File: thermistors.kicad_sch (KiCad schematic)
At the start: 10 parts, among them J3 THERM_1, J4 THERM_2, U7 TCA9535PWR

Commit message: bom: Cleanup some BOM fields
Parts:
- J3: value THERM_1 -> Conn_02x10_Odd_Even
- J4: value THERM_2 -> Conn_02x10_Odd_Even
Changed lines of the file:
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@@
 			)
 		)
-		(property "Value" "THERM_1"
+		(property "Value" "Conn_02x10_Odd_Even"
 			(at 209.55 69.85 0)
 			(effects
@@
 			)
 		)
-		(property "Value" "THERM_2"
+		(property "Value" "Conn_02x10_Odd_Even"
 			(at 209.55 97.79 0)
 			(effects

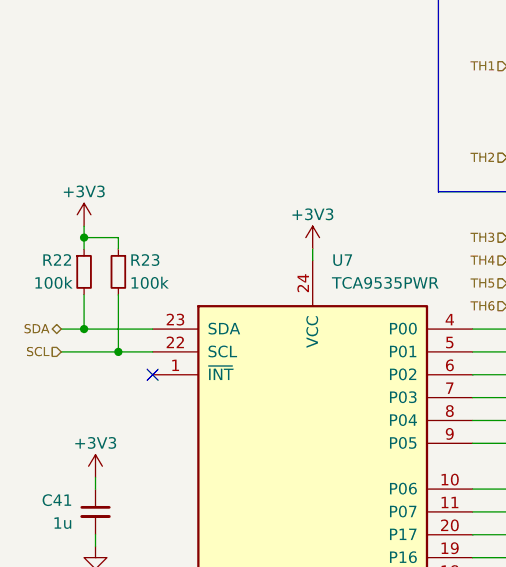
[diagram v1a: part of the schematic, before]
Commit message: schematic: Change all 100k resistors to 10k
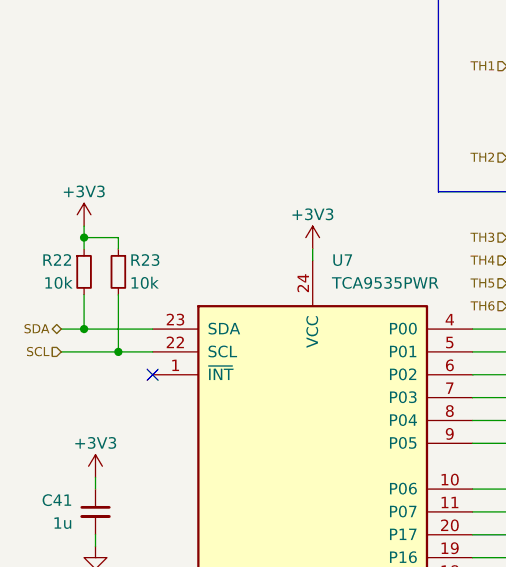
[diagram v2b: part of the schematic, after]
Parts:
- R22, R23: value 100k -> 10k; Dist # C25803 -> C25804; Mfr # 0603WAF1003T5E -> 0603WAF1002T5E
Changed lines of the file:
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@@
 			)
 		)
-		(property "Value" "100k"
+		(property "Value" "10k"
 			(at 153.67 78.74 0)
 			(effects
@@
 			)
 		)
-		(property "Dist #" "C25803"
+		(property "Dist #" "C25804"
 			(at 154.94 77.47 0)
 			(effects
@@
 			)
 		)
-		(property "Mfr #" "0603WAF1003T5E"
+		(property "Mfr #" "0603WAF1002T5E"
 			(at 154.94 77.47 0)
 			(effects
@@
 			)
 		)
-		(property "Value" "100k"
+		(property "Value" "10k"
 			(at 160.02 78.74 0)
 			(effects
@@
 			)
 		)
-		(property "Dist #" "C25803"
+		(property "Dist #" "C25804"
 			(at 158.75 77.47 0)
 			(effects
@@
 			)
 		)
-		(property "Mfr #" "0603WAF1003T5E"
-			(at 158.75 77.47 0)
-			(effects
+		(property "Mfr #" "0603WAF1002T5E"
+			(at 158.75 77.47 0)
+			(effects

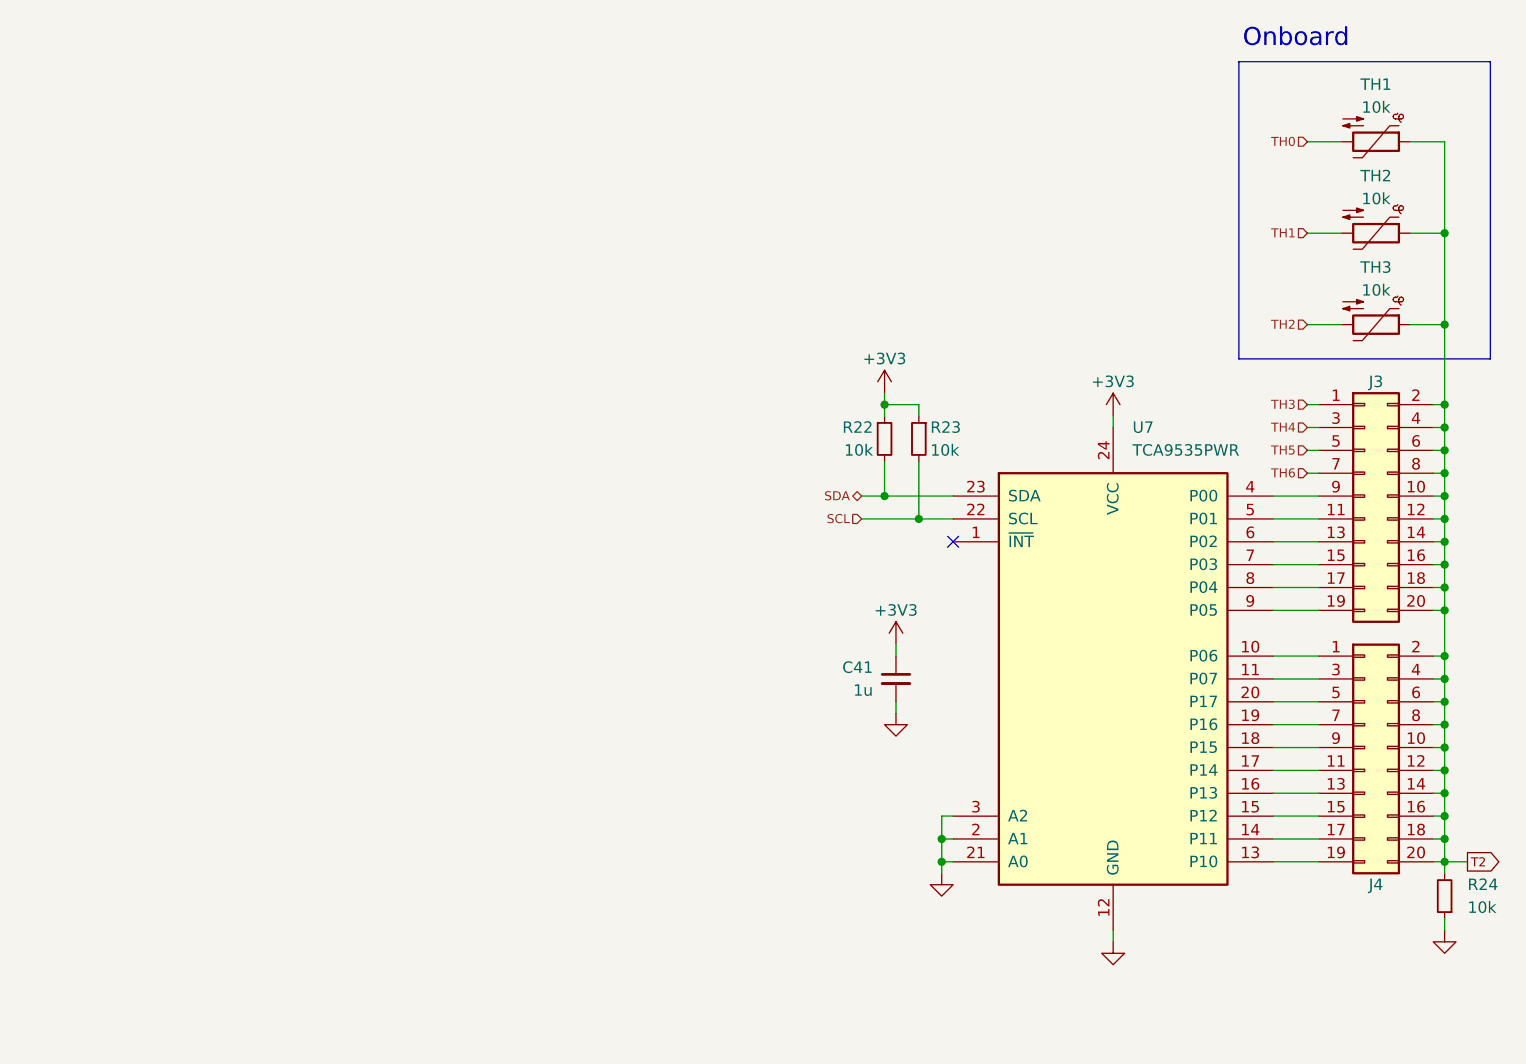
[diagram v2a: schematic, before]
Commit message: schematic: Rework thermistor frontend
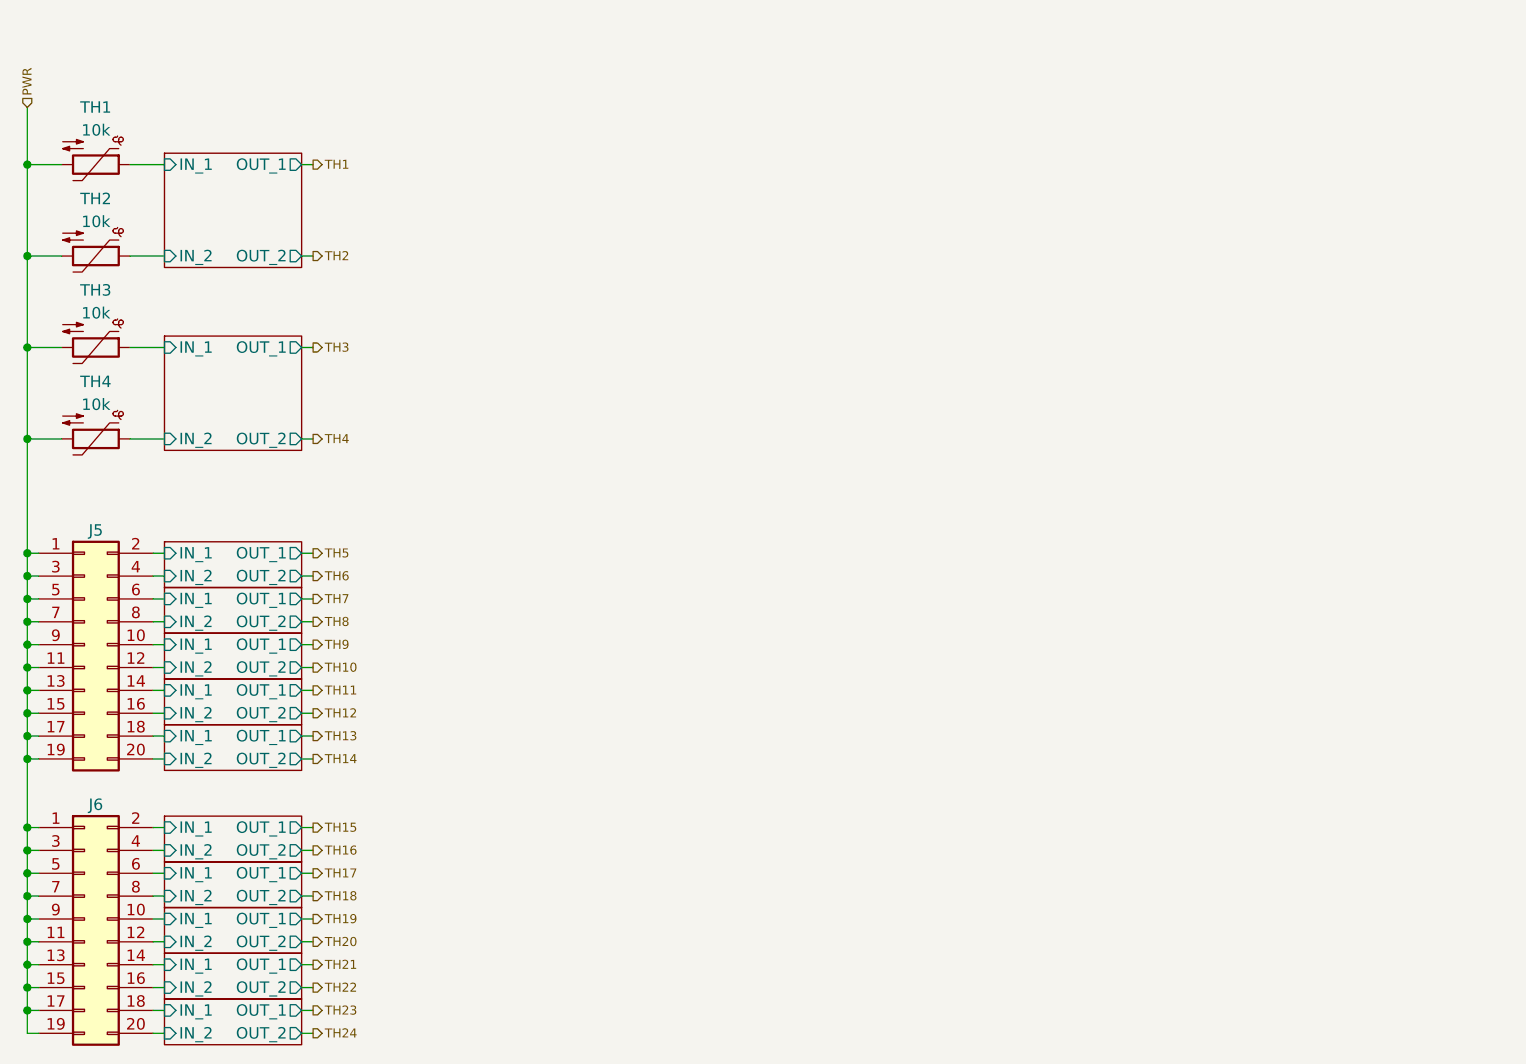
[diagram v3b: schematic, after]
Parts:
- removed C41: 1u, Capacitor_SMD:C_0603_1608Metric, symbol Device:C_Small
- removed J3, J4: Conn_02x10_Odd_Even, Connector_JST:JST_PUD_S20B-PUDSS-1_2x10_P2.00mm_Horizontal, symbol Connector_Generic:Conn_02x10_Odd_Even
- removed R22, R23, R24: 10k, Resistor_SMD:R_0603_1608Metric, symbol Device:R_Small
- removed U7: TCA9535PWR, Package_SO:TSSOP-24_4.4x7.8mm_P0.65mm, symbol Interface_Expansion:TCA9535PWR
- added J5, J6: Conn_02x10_Odd_Even, Connector_JST:JST_PUD_S20B-PUDSS-1_2x10_P2.00mm_Horizontal, symbol Connector_Generic:Conn_02x10_Odd_Even
- added TH4: 10k, Resistor_SMD:R_0603_1608Metric, symbol Device:Thermistor_NTC
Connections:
- net TH1: no longer TH2.2
- net TH2: no longer TH3.2
- removed net T2: TH1.1, TH2.1, TH3.1
- net TH0 renamed PWR
- net PWR: now also TH2.2, TH3.2, J5.1 (Pin_1), J5.11 (Pin_11), J5.13 (Pin_13), J5.15 (Pin_15), J5.17 (Pin_17), J5.19 (Pin_19), J5.3 (Pin_3), J5.5 (Pin_5), J5.7 (Pin_7), J5.9 (Pin_9), J6.1 (Pin_1), J6.11 (Pin_11), J6.13 (Pin_13), J6.15 (Pin_15), J6.17 (Pin_17), J6.19 (Pin_19), J6.3 (Pin_3), J6.5 (Pin_5), J6.7 (Pin_7), J6.9 (Pin_9), TH4.2
- new net Network/IN_1: TH1.1
- new net Network/IN_2: TH2.1
- new net Network1/IN_1: TH3.1
- new net Network1/IN_2: TH4.1
- new net Network10/IN_1: J6.14 (Pin_14)
- new net Network10/IN_2: J6.16 (Pin_16)
- new net Network11/IN_1: J6.18 (Pin_18)
- new net Network11/IN_2: J6.20 (Pin_20)
- new net Network2/IN_1: J5.2 (Pin_2)
- new net Network2/IN_2: J5.4 (Pin_4)
- new net Network3/IN_1: J5.6 (Pin_6)
- new net Network3/IN_2: J5.8 (Pin_8)
- new net Network4/IN_1: J5.10 (Pin_10)
- new net Network4/IN_2: J5.12 (Pin_12)
- new net Network5/IN_1: J5.14 (Pin_14)
- new net Network5/IN_2: J5.16 (Pin_16)
- new net Network6/IN_1: J5.18 (Pin_18)
- new net Network6/IN_2: J5.20 (Pin_20)
- new net Network7/IN_1: J6.2 (Pin_2)
- new net Network7/IN_2: J6.4 (Pin_4)
- new net Network8/IN_1: J6.6 (Pin_6)
- new net Network8/IN_2: J6.8 (Pin_8)
- new net Network9/IN_1: J6.10 (Pin_10)
- new net Network9/IN_2: J6.12 (Pin_12)
- no-connect marks 1 -> 0
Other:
- added sheet Network (thermistor_network.kicad_sch)
- added sheet Network1 (thermistor_network.kicad_sch)
- added sheet Network10 (thermistor_network.kicad_sch)
- added sheet Network11 (thermistor_network.kicad_sch)
- added sheet Network2 (thermistor_network.kicad_sch)
- added sheet Network3 (thermistor_network.kicad_sch)
- added sheet Network4 (thermistor_network.kicad_sch)
- added sheet Network5 (thermistor_network.kicad_sch)
- added sheet Network6 (thermistor_network.kicad_sch)
- added sheet Network7 (thermistor_network.kicad_sch)
- added sheet Network8 (thermistor_network.kicad_sch)
- added sheet Network9 (thermistor_network.kicad_sch)
- note removed: "Onboard"
- title: Battery Management System -> (none)

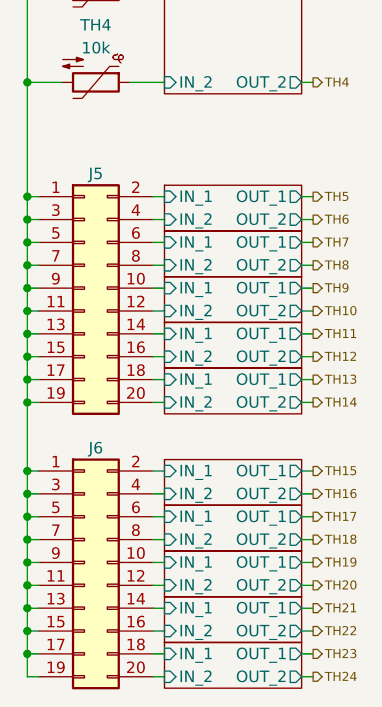
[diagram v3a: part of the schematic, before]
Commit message: schematic: Add board interconnect connectors
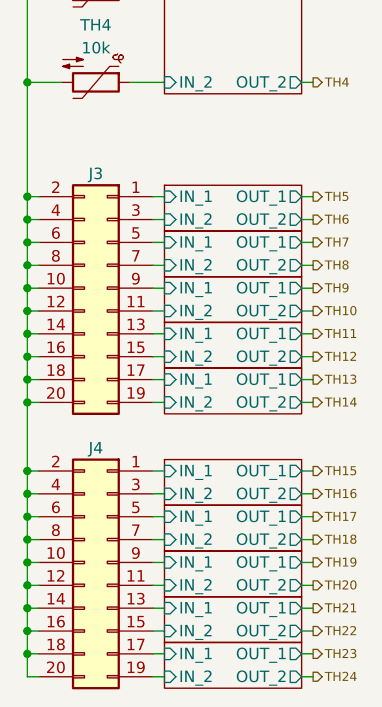
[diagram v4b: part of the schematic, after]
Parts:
- renumbered J5 to J3, J6 to J4
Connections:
- net Network10/IN_1: now also J4.13 (Pin_13); no longer J4.14 (Pin_14)
- net Network10/IN_2: now also J4.15 (Pin_15); no longer J4.16 (Pin_16)
- net Network11/IN_1: now also J4.17 (Pin_17); no longer J4.18 (Pin_18)
- net Network11/IN_2: now also J4.19 (Pin_19); no longer J4.20 (Pin_20)
- net Network2/IN_1: now also J3.1 (Pin_1); no longer J3.2 (Pin_2)
- net Network2/IN_2: now also J3.3 (Pin_3); no longer J3.4 (Pin_4)
- net Network3/IN_1: now also J3.5 (Pin_5); no longer J3.6 (Pin_6)
- net Network3/IN_2: now also J3.7 (Pin_7); no longer J3.8 (Pin_8)
- net Network4/IN_1: now also J3.9 (Pin_9); no longer J3.10 (Pin_10)
- net Network4/IN_2: now also J3.11 (Pin_11); no longer J3.12 (Pin_12)
- net Network5/IN_1: now also J3.13 (Pin_13); no longer J3.14 (Pin_14)
- net Network5/IN_2: now also J3.15 (Pin_15); no longer J3.16 (Pin_16)
- net Network6/IN_1: now also J3.17 (Pin_17); no longer J3.18 (Pin_18)
- net Network6/IN_2: now also J3.19 (Pin_19); no longer J3.20 (Pin_20)
- net Network7/IN_1: now also J4.1 (Pin_1); no longer J4.2 (Pin_2)
- net Network7/IN_2: now also J4.3 (Pin_3); no longer J4.4 (Pin_4)
- net Network8/IN_1: now also J4.5 (Pin_5); no longer J4.6 (Pin_6)
- net Network8/IN_2: now also J4.7 (Pin_7); no longer J4.8 (Pin_8)
- net Network9/IN_1: now also J4.9 (Pin_9); no longer J4.10 (Pin_10)
- net Network9/IN_2: now also J4.11 (Pin_11); no longer J4.12 (Pin_12)
- net PWR: now also J3.10 (Pin_10), J3.12 (Pin_12), J3.14 (Pin_14), J3.16 (Pin_16), J3.18 (Pin_18), J3.2 (Pin_2), J3.20 (Pin_20), J3.4 (Pin_4), J3.6 (Pin_6), J3.8 (Pin_8), J4.10 (Pin_10), J4.12 (Pin_12), J4.14 (Pin_14), J4.16 (Pin_16), J4.18 (Pin_18), J4.2 (Pin_2), J4.20 (Pin_20), J4.4 (Pin_4), J4.6 (Pin_6), J4.8 (Pin_8); no longer J3.1 (Pin_1), J3.11 (Pin_11), J3.13 (Pin_13), J3.15 (Pin_15), J3.17 (Pin_17), J3.19 (Pin_19), J3.3 (Pin_3), J3.5 (Pin_5), J3.7 (Pin_7), J3.9 (Pin_9), J4.1 (Pin_1), J4.11 (Pin_11), J4.13 (Pin_13), J4.15 (Pin_15), J4.17 (Pin_17), J4.19 (Pin_19), J4.3 (Pin_3), J4.5 (Pin_5), J4.7 (Pin_7), J4.9 (Pin_9)
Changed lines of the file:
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@@
 	(symbol
 		(lib_id "Connector_Generic:Conn_02x10_Odd_Even")
-		(at 66.04 100.33 0)
+		(at 68.58 100.33 0)
+		(mirror y)
 		(unit 1)
 		(exclude_from_sim no)
@@
 		(on_board yes)
 		(dnp no)
-		(property "Reference" "J5"
+		(property "Reference" "J3"
 			(at 67.31 87.63 0)
 			(effects
@@
 		)
 		(property "Footprint" "Connector_JST:JST_PUD_S20B-PUDSS-1_2x10_P2.00mm_Horizontal"
-			(at 66.04 100.33 0)
+			(at 68.58 100.33 0)
 			(effects
 				(font
@@
 		)
 		(property "Datasheet" "~"
-			(at 66.04 100.33 0)
+			(at 68.58 100.33 0)
 			(effects
 				(font
@@
 		)
 		(property "Description" "Generic connector, double row, 02x10, odd/even pin numbering scheme (row 1 odd numbers, row 2 even numbers), script generated (kicad-library-utils/schlib/autogen/connector/)"
-			(at 66.04 100.33 0)
+			(at 68.58 100.33 0)
 			(effects
 				(font
@@
 		)
 		(property "Dist #" "C495200"
-			(at 66.04 100.33 0)
+			(at 68.58 100.33 0)
 			(effects
 				(font
@@
 		)
 		(property "Mfr" "JST"
-			(at 66.04 100.33 0)
+			(at 68.58 100.33 0)
 			(effects
 				(font
@@
 		)
 		(property "Mfr #" "S20B-PUDSS-1(LF)(SN)"
-			(at 66.04 100.33 0)
+			(at 68.58 100.33 0)
 			(effects
 				(font
@@
 		)
 		(property "Dist" "LCSC"
-			(at 66.04 100.33 0)
+			(at 68.58 100.33 0)
 			(effects
 				(font
@@
 			(project "bms_segment"
 				(path "/ae4a7653-8e6d-4e05-b144-1e5e3b2092b7/8e615871-66d5-4c39-bd5b-a90cbe433475/7307489e-20ac-44bd-af31-63baacb8067c"
-					(reference "J5")
+					(reference "J3")
 					(unit 1)
 				)
@@
 	(symbol
 		(lib_id "Connector_Generic:Conn_02x10_Odd_Even")
-		(at 66.04 130.81 0)
+		(at 68.58 130.81 0)
+		(mirror y)
 		(unit 1)
 		(exclude_from_sim no)
@@
 		(on_board yes)
 		(dnp no)
-		(property "Reference" "J6"
+		(property "Reference" "J4"
 			(at 67.31 118.11 0)
 			(effects
@@
 		)
 		(property "Footprint" "Connector_JST:JST_PUD_S20B-PUDSS-1_2x10_P2.00mm_Horizontal"
-			(at 66.04 130.81 0)
+			(at 68.58 130.81 0)
 			(effects
 				(font
@@
 		)
 		(property "Datasheet" "~"
-			(at 66.04 130.81 0)
+			(at 68.58 130.81 0)
 			(effects
 				(font
@@
 		)
 		(property "Description" "Generic connector, double row, 02x10, odd/even pin numbering scheme (row 1 odd numbers, row 2 even numbers), script generated (kicad-library-utils/schlib/autogen/connector/)"
-			(at 66.04 130.81 0)
+			(at 68.58 130.81 0)
 			(effects
 				(font
@@
 		)
 		(property "Dist #" "C495200"
-			(at 66.04 130.81 0)
+			(at 68.58 130.81 0)
 			(effects
 				(font
@@
 		)
 		(property "Mfr" "JST"
-			(at 66.04 130.81 0)
+			(at 68.58 130.81 0)
 			(effects
 				(font
@@
 		)
 		(property "Mfr #" "S20B-PUDSS-1(LF)(SN)"
-			(at 66.04 130.81 0)
+			(at 68.58 130.81 0)
 			(effects
 				(font
@@
 		)
 		(property "Dist" "LCSC"
-			(at 66.04 130.81 0)
+			(at 68.58 130.81 0)
 			(effects
 				(font
@@
 			(project "bms_segment"
 				(path "/ae4a7653-8e6d-4e05-b144-1e5e3b2092b7/8e615871-66d5-4c39-bd5b-a90cbe433475/7307489e-20ac-44bd-af31-63baacb8067c"
-					(reference "J6")
+					(reference "J4")
 					(unit 1)
 				)

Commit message: *: Minor cleanup
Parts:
- renumbered J3 to J2, J4 to J3
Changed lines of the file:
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@@
 		(on_board yes)
 		(dnp no)
-		(property "Reference" "J3"
+		(property "Reference" "J2"
 			(at 67.31 87.63 0)
 			(effects
@@
 			(project "bms_segment"
 				(path "/ae4a7653-8e6d-4e05-b144-1e5e3b2092b7/8e615871-66d5-4c39-bd5b-a90cbe433475/7307489e-20ac-44bd-af31-63baacb8067c"
-					(reference "J3")
+					(reference "J2")
 					(unit 1)
 				)
@@
 		(on_board yes)
 		(dnp no)
-		(property "Reference" "J4"
+		(property "Reference" "J3"
 			(at 67.31 118.11 0)
 			(effects
@@
 			(project "bms_segment"
 				(path "/ae4a7653-8e6d-4e05-b144-1e5e3b2092b7/8e615871-66d5-4c39-bd5b-a90cbe433475/7307489e-20ac-44bd-af31-63baacb8067c"
-					(reference "J4")
+					(reference "J3")
 					(unit 1)
 				)

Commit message: *: Rework BOM
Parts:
- J2, J3: DigiKey # (none) -> 455-S20B-PUDSS-1-ND; Dist LCSC -> (none); Dist # C495200 -> (none); LCSC # (none) -> C495200; Mouser # (none) -> 306-S20BPUDSS1LFSN
- TH1, TH2, TH3, TH4: DigiKey # (none) -> 490-4800-1-ND; Dist LCSC -> (none); Dist # C13564 -> (none); LCSC # (none) -> C13564; Mouser # (none) -> 81-NCP18XH103F03RB
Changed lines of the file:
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@@
-			)
-		)
-		(property "Dist #" "C13564"
-			(at 67.31 57.15 0)
-			(effects
-				(font
-					(size 1.27 1.27)
-				)
-				(hide yes)
 			)
 		)
@@
 			)
 		)
-		(property "Dist" "LCSC"
-			(at 67.31 57.15 0)
+		(property "DigiKey #" "490-4800-1-ND"
+			(at 67.31 57.15 90)
+			(effects
+				(font
+					(size 1.27 1.27)
+				)
+				(hide yes)
+			)
+		)
+		(property "LCSC #" "C13564"
+			(at 67.31 57.15 90)
+			(effects
+				(font
+					(size 1.27 1.27)
+				)
+				(hide yes)
+			)
+		)
+		(property "Mouser #" "81-NCP18XH103F03RB"
+			(at 67.31 57.15 90)
 			(effects
 				(font
@@
 			)
 		)
-		(property "Dist #" "C13564"
-			(at 67.31 67.31 0)
-			(effects
-				(font
-					(size 1.27 1.27)
-				)
-				(hide yes)
-			)
-		)
 		(property "Mfr" "Murata"
 			(at 67.31 67.31 0)
@@
 			)
 		)
-		(property "Dist" "LCSC"
-			(at 67.31 67.31 0)
+		(property "DigiKey #" "490-4800-1-ND"
+			(at 67.31 67.31 90)
+			(effects
+				(font
+					(size 1.27 1.27)
+				)
+				(hide yes)
+			)
+		)
+		(property "LCSC #" "C13564"
+			(at 67.31 67.31 90)
+			(effects
+				(font
+					(size 1.27 1.27)
+				)
+				(hide yes)
+			)
+		)
+		(property "Mouser #" "81-NCP18XH103F03RB"
+			(at 67.31 67.31 90)
 			(effects
 				(font
@@
 			)
 		)
-		(property "Dist #" "C13564"
-			(at 67.31 77.47 0)
-			(effects
-				(font
-					(size 1.27 1.27)
-				)
-				(hide yes)
-			)
-		)
 		(property "Mfr" "Murata"
 			(at 67.31 77.47 0)
@@
 			)
 		)
-		(property "Dist" "LCSC"
-			(at 67.31 77.47 0)
+		(property "DigiKey #" "490-4800-1-ND"
+			(at 67.31 77.47 90)
+			(effects
+				(font
+					(size 1.27 1.27)
+				)
+				(hide yes)
+			)
+		)
+		(property "LCSC #" "C13564"
+			(at 67.31 77.47 90)
+			(effects
+				(font
+					(size 1.27 1.27)
+				)
+				(hide yes)
+			)
+		)
+		(property "Mouser #" "81-NCP18XH103F03RB"
+			(at 67.31 77.47 90)
 			(effects
 				(font
@@
 			)
 		)
-		(property "Dist #" "C13564"
-			(at 67.31 46.99 0)
-			(effects
-				(font
-					(size 1.27 1.27)
-				)
-				(hide yes)
-			)
-		)
 		(property "Mfr" "Murata"
 			(at 67.31 46.99 0)
@@
 			)
 		)
-		(property "Dist" "LCSC"
-			(at 67.31 46.99 0)
+		(property "DigiKey #" "490-4800-1-ND"
+			(at 67.31 46.99 90)
+			(effects
+				(font
+					(size 1.27 1.27)
+				)
+				(hide yes)
+			)
+		)
+		(property "LCSC #" "C13564"
+			(at 67.31 46.99 90)
+			(effects
+				(font
+					(size 1.27 1.27)
+				)
+				(hide yes)
+			)
+		)
+		(property "Mouser #" "81-NCP18XH103F03RB"
+			(at 67.31 46.99 90)
 			(effects
 				(font
@@
 			)
 		)
-		(property "Dist #" "C495200"
-			(at 68.58 100.33 0)
-			(effects
-				(font
-					(size 1.27 1.27)
-				)
-				(hide yes)
-			)
-		)
 		(property "Mfr" "JST"
 			(at 68.58 100.33 0)
@@
 			)
 		)
-		(property "Dist" "LCSC"
+		(property "DigiKey #" "455-S20B-PUDSS-1-ND"
+			(at 68.58 100.33 0)
+			(effects
+				(font
+					(size 1.27 1.27)
+				)
+				(hide yes)
+			)
+		)
+		(property "LCSC #" "C495200"
+			(at 68.58 100.33 0)
+			(effects
+				(font
+					(size 1.27 1.27)
+				)
+				(hide yes)
+			)
+		)
+		(property "Mouser #" "306-S20BPUDSS1LFSN"
 			(at 68.58 100.33 0)
 			(effects
@@
 			)
 		)
-		(property "Dist #" "C495200"
-			(at 68.58 130.81 0)
-			(effects
-				(font
-					(size 1.27 1.27)
-				)
-				(hide yes)
-			)
-		)
 		(property "Mfr" "JST"
 			(at 68.58 130.81 0)
@@
 			)
 		)
-		(property "Dist" "LCSC"
-			(at 68.58 130.81 0)
-			(effects
+		(property "DigiKey #" "455-S20B-PUDSS-1-ND"
+			(at 68.58 130.81 0)
+			(effects
+				(font
+					(size 1.27 1.27)
+				)
+				(hide yes)
+			)
+		)
+		(property "LCSC #" "C495200"
+			(at 68.58 130.81 0)
+			(effects
+				(font
+					(size 1.27 1.27)
+				)
+				(hide yes)
+			)
+		)
+		(property "Mouser #" "306-S20BPUDSS1LFSN"
+			(at 68.58 130.81 0)
+			(effects
